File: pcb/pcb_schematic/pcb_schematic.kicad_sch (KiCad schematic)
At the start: 24 parts, among them J1 Conn_ST_STDC14, J2 USB_B_Micro, J3 Conn_02x02_Odd_Even, U1 STM32G031K8Tx, U2 MIC5301-3.3YD5, U4 SSD1306 128 x 64 OLED (0x3C), U5 TCS34725 (0x29), Y1 Crystal

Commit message: oct 22
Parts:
- removed CR1, CR2: LSM115JE3/TR13, _custom:DO-214BA_MCH, symbol _custom:LSM115JE3_TR13
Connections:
- net VBUS: now also C7.2, U2.1 (VIN), U2.3 (EN)
- net at J1.6 (JCLK/SWCLK), U1.25 (PA14): no longer U1.26 (PA15)
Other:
- note removed: "C3757764"
- note removed: "Schottky < 300mV"
- moved on the sheet: C3, C4, J1, J3, U1, Y1

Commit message: ht
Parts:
- added C6: 0.1uF, Capacitor_SMD:C_0603_1608Metric, symbol Device:C_Small
- added SW1: Reset, Button_Switch_SMD:SW_SPST_B3U-1000P, symbol Switch:SW_Push
- U4: footprint DM-OLED096-636:MODULE_DM-OLED096-636 -> SSD1306:128x64OLED
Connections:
- net GND: now also C6.2, SW1.2
- net INT: now reaches U1.11 (PA4)
- net INT: now also U5.6 (INT)
- net at U1.6 (PF2): now also J1.12 (~{RST}), C6.1, SW1.1
- no-connect marks 25 -> 26
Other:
- note added: "C231330"
- note added: "~40K Internal PU CAP Must be close to chip (5.3.15)"
- moved on the sheet: C3, C4, J1, J3, U1, Y1

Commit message: bluh
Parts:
- removed C6: 0.1uF, Capacitor_SMD:C_0603_1608Metric, symbol Device:C_Small
- removed SW1: Reset, Button_Switch_SMD:SW_SPST_B3U-1000P, symbol Switch:SW_Push
- added C1: 4.7uF, Capacitor_SMD:C_0805_2012Metric, symbol Device:C_Small
- C10, C7: footprint Capacitor_SMD:C_1206_3216Metric -> Capacitor_SMD:C_0805_2012Metric
- C11, C12, C3, C4: footprint Capacitor_SMD:C_0603_1608Metric -> Capacitor_SMD:C_0805_2012Metric
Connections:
- net +3.3V: now also C1.1
- net GND: now also C1.2
- net LED: now reaches U1.12 (PA5)
- net LED: now also U5.7 (LED)
- no-connect marks 26 -> 24
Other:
- note added: "MCU Bypass Ceramic"
- note removed: "C231330"
- note removed: "~40K Internal PU CAP Must be close to chip (5.3.15)"
- moved on the sheet: C12

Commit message: v4 now?
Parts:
- J1: footprint (none) -> Connector_PinHeader_1.27mm:PinHeader_2x07_P1.27mm_Vertical_SMD
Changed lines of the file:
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@@
 			)
 		)
-		(property "Footprint" ""
+		(property "Footprint" "Connector_PinHeader_1.27mm:PinHeader_2x07_P1.27mm_Vertical_SMD"
 			(at 156.21 41.91 0)
 			(effects

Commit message: almost checkoff
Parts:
- added C2: 4.7uF, Capacitor_SMD:C_0805_2012Metric, symbol Device:C_Small
- added D1: CLMVC-FKA-CLBDGL7LBB79353, CLMVC-FKA-CLBDGL7LBB79353:LED_CLMVC-FKA-CLBDGL7LBB79353, symbol CLMVC-FKA-CLBDGL7LBB79353:CLMVC-FKA-CLBDGL7LBB79353
- added Q1, Q2, Q3: MMBT3904, Package_TO_SOT_SMD:SOT-23, symbol Transistor_BJT:MMBT3904
- added R10, R8, R9: 10k, Resistor_SMD:R_0805_2012Metric, symbol Device:R_Small_US
- added R5: 1k, Resistor_SMD:R_0805_2012Metric, symbol Device:R_Small_US
- added R6: 1.1k, Resistor_SMD:R_0805_2012Metric, symbol Device:R_Small_US
- added R7: 330, Resistor_SMD:R_0805_2012Metric, symbol Device:R_Small_US
- C1: value 4.7uF -> 1uF
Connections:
- net +3.3V: now also C2.1, D1.1
- net GND: now also C2.2, Q1.2 (E), Q2.2 (E), Q3.2 (E)
- net PWM1: now reaches U1.13 (PA6)
- net PWM1: now also R8.1
- net PWM2: now reaches U1.14 (PA7)
- net PWM2: now also R9.1
- net PWM3: now reaches U1.18 (PA8)
- net PWM3: now also R10.1
- new net: D1.4, R7.1
- new net: Q3.3 (C), R7.2
- new net: D1.2, R5.1
- new net: D1.3, R6.1
- new net: Q2.3 (C), R6.2
- new net: Q1.1 (B), R8.2
- new net: Q1.3 (C), R5.2
- no-connect marks 24 -> 21
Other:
- note added: "Disconnect power to RESET"
- moved on the sheet: C1, C3, C4, Y1

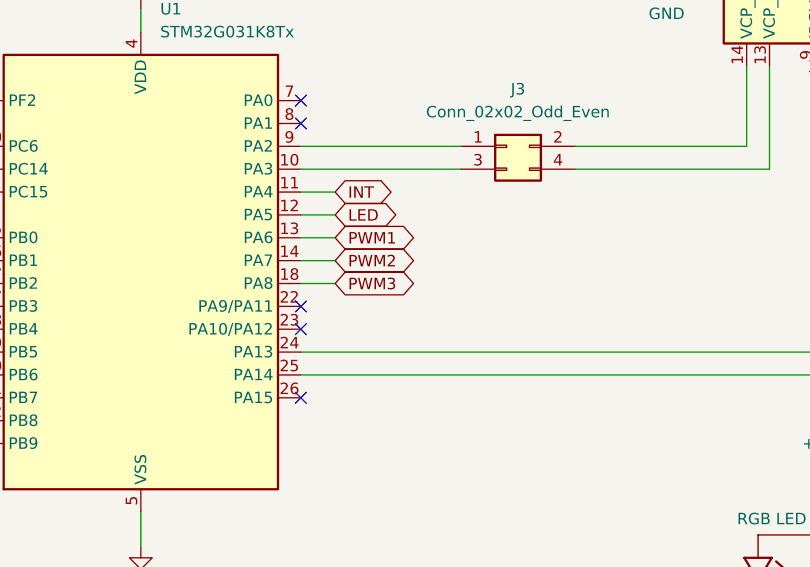
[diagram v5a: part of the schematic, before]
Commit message: PWM on Timer 1 Pins
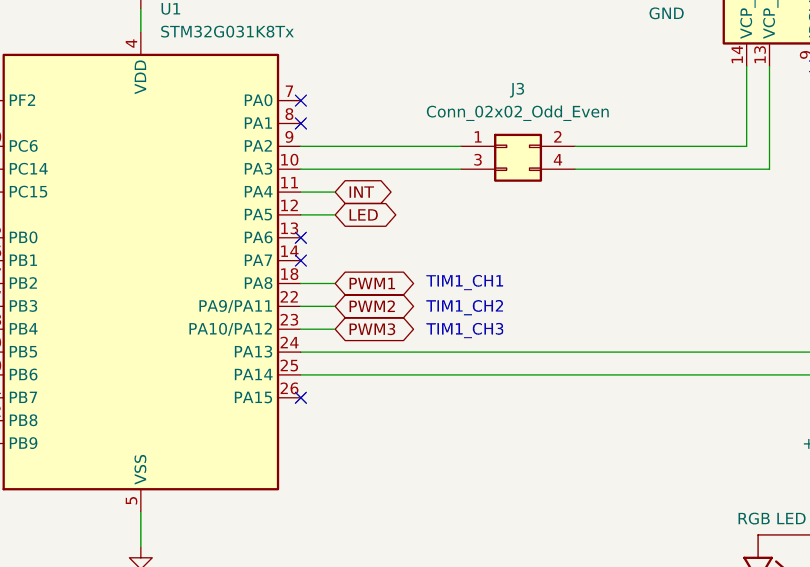
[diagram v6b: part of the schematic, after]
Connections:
- net PWM1: now also U1.18 (PA8); no longer U1.13 (PA6)
- net PWM2: now also U1.22 (PA9/PA11); no longer U1.14 (PA7)
- net PWM3: now also U1.23 (PA10/PA12); no longer U1.18 (PA8)
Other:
- note added: "TIM1_CH1"
- note added: "TIM1_CH2"
- note added: "TIM1_CH3"

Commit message: the schmatic keeps chaning i wanna cry
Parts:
- removed C10, C7: 1uF CER, Capacitor_SMD:C_0805_2012Metric, symbol Device:C
- removed C5: 4.7nF 1KV, Capacitor_SMD:C_0805_2012Metric, symbol Device:C_Small
- removed C9: 0.01uF, Capacitor_SMD:C_0805_2012Metric, symbol Device:C_Small
- removed J2: USB_B_Micro, Connector_USB:USB_Micro-B_Amphenol_10118194_Horizontal, symbol Connector:USB_B_Micro
- removed R1: 1M, Resistor_SMD:R_0805_2012Metric, symbol Device:R_Small_US
- removed R11: 10K, Resistor_SMD:R_0805_2012Metric, symbol Device:R_Small_US
- removed U2: MIC5301-3.3YD5, Package_TO_SOT_SMD:TSOT-23-5, symbol _custom:MIC5301
- added C14, C8: 10uF, Capacitor_SMD:C_0805_2012Metric, symbol Device:C
- added C6: 4.7nF 1KV, Capacitor_SMD:C_0805_2012Metric, symbol Device:C_Small
- added J4: USB_B_Micro, Connector_USB:USB_Micro-B_Amphenol_10118194_Horizontal, symbol Connector:USB_B_Micro
- added R12: 10K, Resistor_SMD:R_0805_2012Metric, symbol Device:R_Small_US
- added R2: 1M, Resistor_SMD:R_0805_2012Metric, symbol Device:R_Small_US
- added U2: NCP1117-3.3_SOT223, Package_TO_SOT_SMD:SOT-223-3_TabPin2, symbol Regulator_Linear:NCP1117-3.3_SOT223
- R5: value 1k -> 470
- R6: value 1.1k -> 220
- R7: value 330 -> 51
- U4: now not fitted
- U5: footprint (none) -> Sensor:TCS34725; now not fitted
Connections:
- net +3.3V: now also C14.2, U2.2 (VO)
- net GND: now also C14.1, C6.2, C8.1, J4.5 (GND), R12.1, R2.2, U2.1 (GND)
- net VBUS: now also C8.2, J4.1 (VBUS), R12.2, U2.3 (VI)
- net at R10.2: now also Q3.1 (B)
- net at R9.2: now also Q2.1 (B)
- new net: C6.1, J4.6 (Shield), R2.1
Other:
- note removed: "Must be ULDO"

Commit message: Created pcb desgin, need to rid of all warning
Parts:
- J3: now not fitted
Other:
- moved on the sheet: C1, C2, C3, C4, U1, Y1
